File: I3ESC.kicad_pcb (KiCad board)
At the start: 4 copper layers, 64 x 54 mm, 155 parts, among them J1 JST SR/SZ, J10 VIN_BARREL, J11 VIN_BARREL, J12 JST SR/SZ, J13 Conn_01x03, J2 Screw_Terminal_01x02, J3 Screw_Terminal_01x02, J4 Screw_Terminal_01x02, J5 Encoder, J6 Screw_Terminal_01x02, J7 Screw_Terminal_01x02, J8 Encoder, J9 JST SR/SZ, SW1 button, SW2 button, SW3 button, U1 SY8113BADC, U10 USBLC6-2P6, U11 Qwiic2, U12 FD8288T (DRV8300), U2 FD8288T (DRV8300), U3 SPX3819M5-L-3-3, U4 STM32G474RETx, U5 Qwiic1, U8 ABM3B-8.000MHZ, U9 USB_C_Receptacle

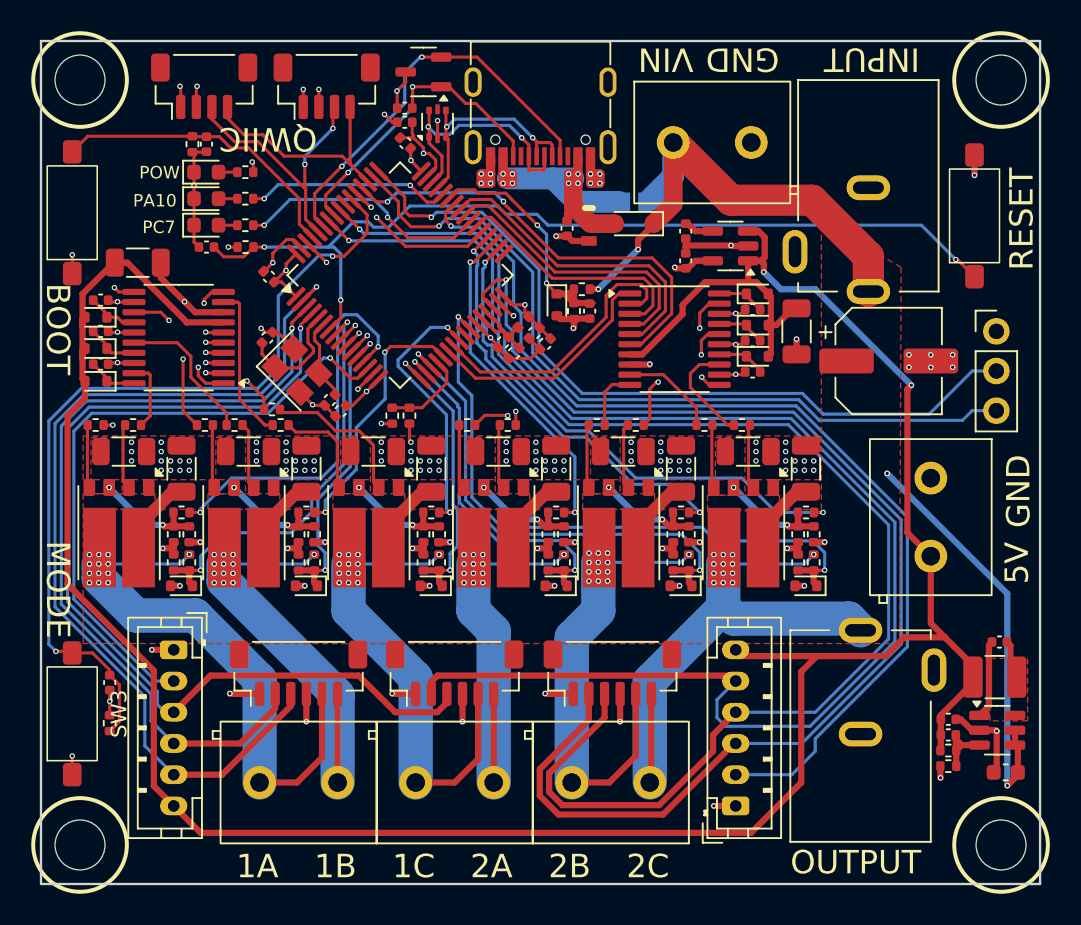
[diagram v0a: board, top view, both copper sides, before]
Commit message: fixed LCSC Numbers, order 9-10-26
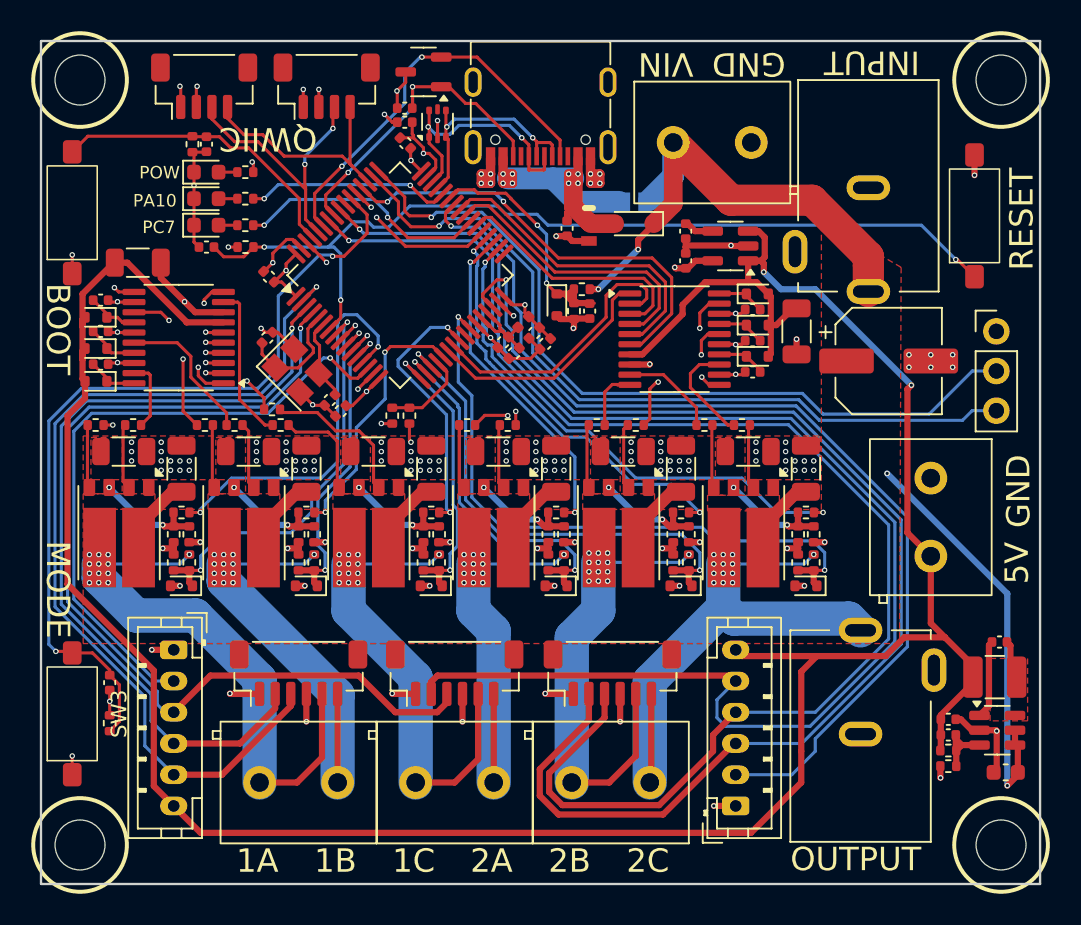
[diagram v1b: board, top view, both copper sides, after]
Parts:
- added REF**: Tab, PCM_kikit:Tab, F.Cu at (20.0, -27.2)
- added REF**: Tab, PCM_kikit:Tab, F.Cu at (20.0, 27.2)
- added REF**: Tab, PCM_kikit:Tab, F.Cu at (-20.0, -27.2)
- added REF**: Tab, PCM_kikit:Tab, F.Cu at (-20.0, 27.2)
- U11: value Qwiic2 -> Qwiic
- U5: value Qwiic1 -> Qwiic
